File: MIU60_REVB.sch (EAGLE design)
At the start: 80 parts, among them P1 PAD-10G, P2 PAD-10G

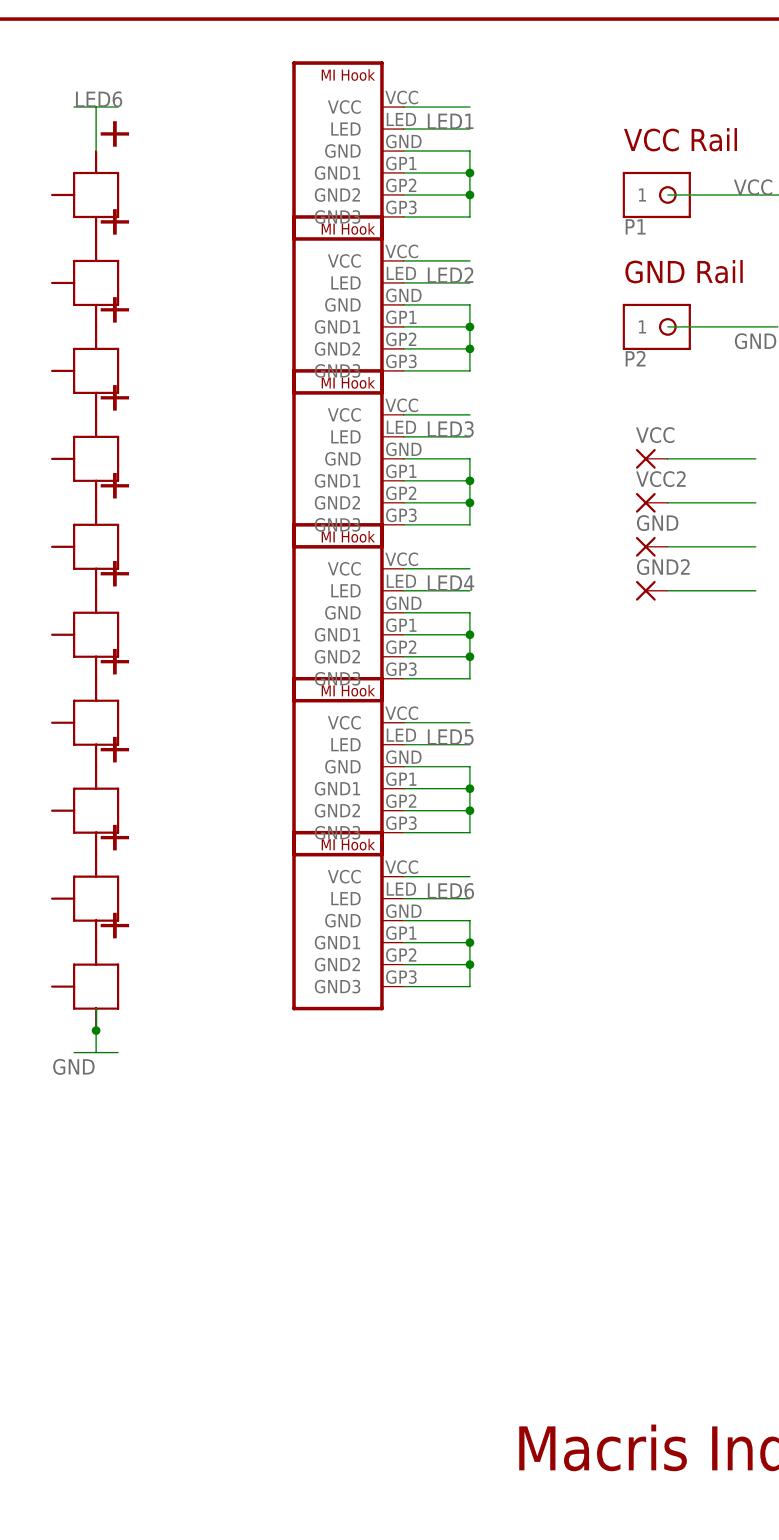
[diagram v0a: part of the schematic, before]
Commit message: Added the final piece in mechanical.lbr for final ground that I for some reason didnt add
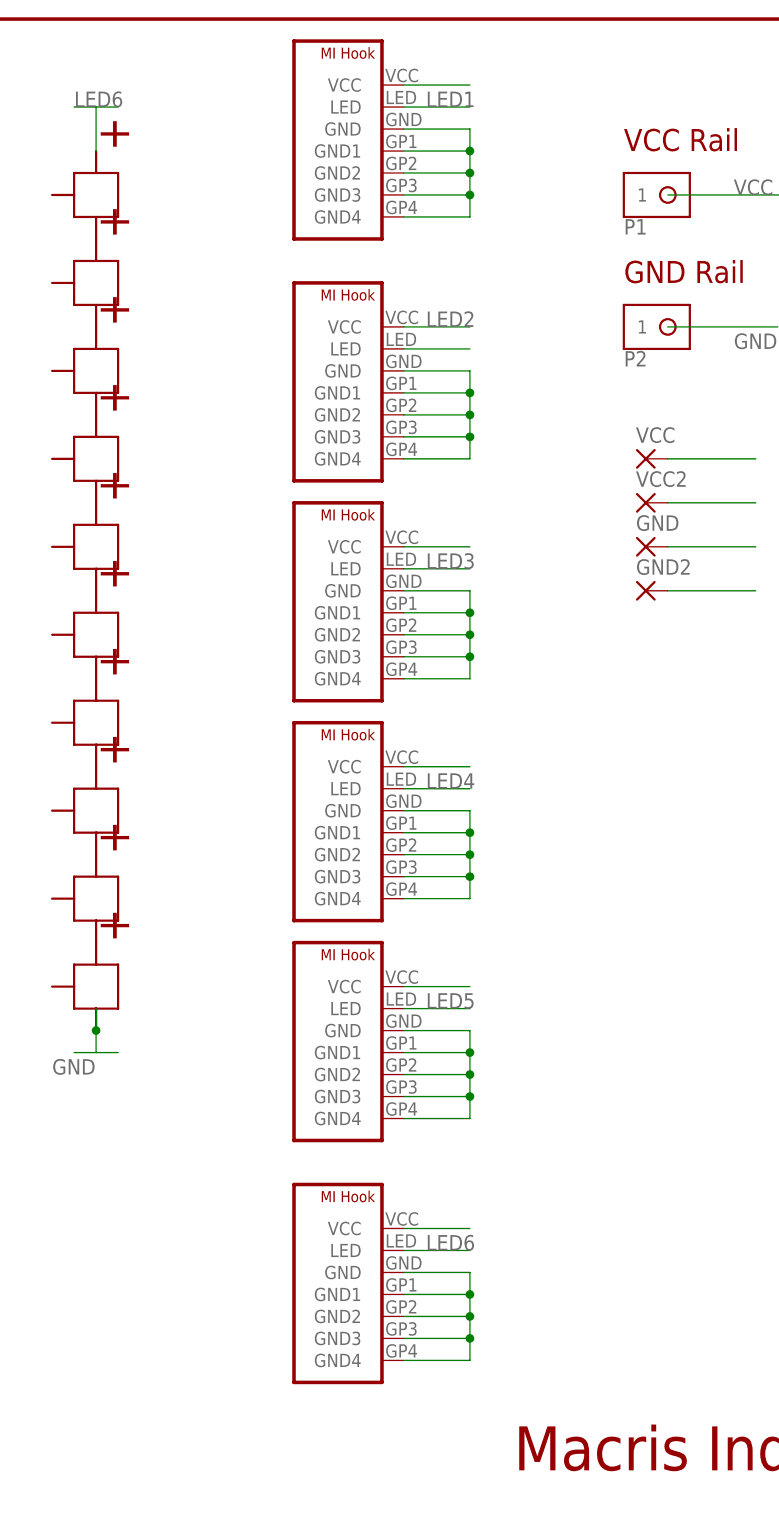
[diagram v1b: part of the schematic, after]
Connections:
- net GND: now also U$10.GND4, U$11.GND4, U$12.GND4, U$13.GND4, U$14.GND4, U$9.GND4
